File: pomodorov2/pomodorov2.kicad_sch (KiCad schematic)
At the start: 13 parts, among them J1 USB_B_Micro, J2 TC2050-IDC, J3 SOICbite, J4 Stemma, U1 MDBT50Q-1MV2, Y1 32.768kHz

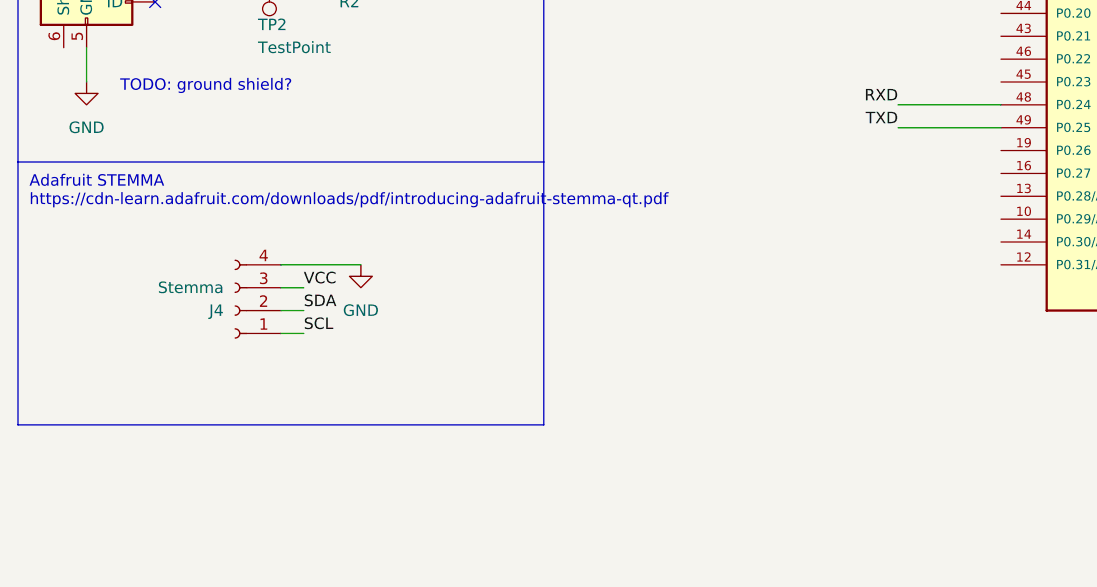
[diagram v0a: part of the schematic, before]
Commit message: Populate parts on board, remove stemma conn 🪓
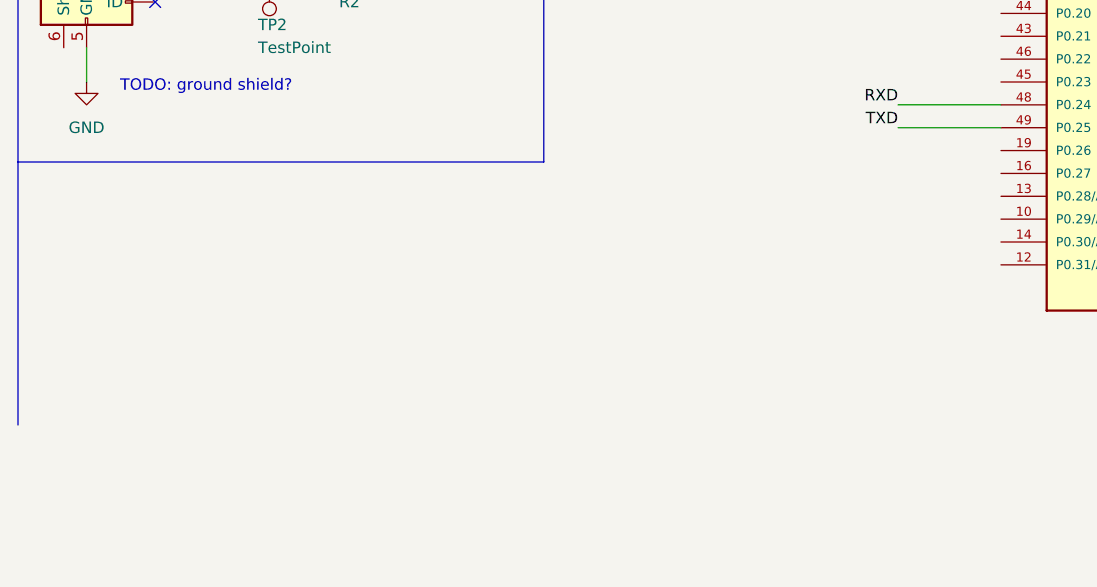
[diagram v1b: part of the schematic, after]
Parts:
- removed J4: Stemma, Connector_JST:JST_PH_S4B-PH-K_1x04_P2.00mm_Horizontal, symbol Connector:Conn_01x04_Female
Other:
- note removed: "Adafruit STEMMA https://cdn-learn.adafruit.com/downloads/pdf/introducing-adafruit-stemma-qt.pdf"
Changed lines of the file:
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@@
-    (stroke (width 0) (type default) (color 0 0 0 0))
-  )
-  (wire (pts (xy 40.64 133.35) (xy 43.18 133.35))
     (stroke (width 0) (type default) (color 0 0 0 0))
   )
@@
     (stroke (width 0) (type default) (color 0 0 0 0))
   )
-  (polyline (pts (xy 69.85 148.59) (xy 69.85 119.38))
-    (stroke (width 0) (type default) (color 0 0 0 0))
-  )
   (wire (pts (xy 109.22 97.79) (xy 120.65 97.79))
     (stroke (width 0) (type default) (color 0 0 0 0))
@@
     (stroke (width 0) (type default) (color 0 0 0 0))
   )
-  (polyline (pts (xy 11.43 148.59) (xy 69.85 148.59))
-    (stroke (width 0) (type default) (color 0 0 0 0))
-  )
   (wire (pts (xy 97.79 46.99) (xy 93.98 46.99))
     (stroke (width 0) (type default) (color 0 0 0 0))
   )
-  (wire (pts (xy 40.64 138.43) (xy 43.18 138.43))
-    (stroke (width 0) (type default) (color 0 0 0 0))
-  )
   (wire (pts (xy 26.67 24.13) (xy 33.02 24.13))
     (stroke (width 0) (type default) (color 0 0 0 0))
@@
     (stroke (width 0) (type default) (color 0 0 0 0))
   )
-  (wire (pts (xy 40.64 135.89) (xy 43.18 135.89))
-    (stroke (width 0) (type default) (color 0 0 0 0))
-  )
   (wire (pts (xy 26.67 67.31) (xy 26.67 72.39))
     (stroke (width 0) (type default) (color 0 0 0 0))
@@
     (stroke (width 0) (type default) (color 0 0 0 0))
   )
-  (wire (pts (xy 40.64 130.81) (xy 49.53 130.81))
-    (stroke (width 0) (type default) (color 0 0 0 0))
-  )
   (text "Maybe ground\n(or N/C)" (at 12.7 73.66 0)
     (effects (font (size 1.27 1.27)) (justify left bottom))
@@
   )
   (text "April 10, 2022" (at 207.01 194.31 0)
-    (effects (font (size 1.27 1.27)) (justify left bottom))
-  )
-  (text "Adafruit STEMMA\nhttps://cdn-learn.adafruit.com/downloads/pdf/introducing-adafruit-stemma-qt.pdf"
-    (at 12.7 124.46 0)
     (effects (font (size 1.27 1.27)) (justify left bottom))
   )
@@
     (effects (font (size 1.27 1.27)) (justify left bottom))
   )
-  (label "SDA" (at 43.18 135.89 0)
-    (effects (font (size 1.27 1.27)) (justify left bottom))
-  )
   (label "MISO" (at 109.22 90.17 180)
     (effects (font (size 1.27 1.27)) (justify right bottom))
-  )
-  (label "SCL" (at 43.18 138.43 0)
-    (effects (font (size 1.27 1.27)) (justify left bottom))
-  )
-  (label "VCC" (at 43.18 133.35 0)
-    (effects (font (size 1.27 1.27)) (justify left bottom))
   )
   (label "RXD" (at 109.22 113.03 180)
@@
     )
     (pin "1")
-  )
-  (symbol (lib_id "Connector:Conn_01x04_Female") (at 35.56 135.89 180) (unit 1)
-    (in_bom yes) (on_board yes) (fields_autoplaced)
-    (property "Reference" "J4" (id 0) (at 34.29 135.8901 0)
-      (effects (font (size 1.27 1.27)) (justify left))
-    )
-    (property "Value" "Stemma" (id 1) (at 34.29 133.3501 0)
-      (effects (font (size 1.27 1.27)) (justify left))
-    )
-    (property "Footprint" "Connector_JST:JST_PH_S4B-PH-K_1x04_P2.00mm_Horizontal" (id 2) (at 35.56 135.89 0)
-      (effects (font (size 1.27 1.27)) hide)
-    )
-    (property "Datasheet" "~" (id 3) (at 35.56 135.89 0)
-      (effects (font (size 1.27 1.27)) hide)
-    )
-    (pin "1")
-    (pin "2")
-    (pin "3")
-    (pin "4")
   )
   (symbol (lib_id "Device:L") (at 182.88 46.99 90) (unit 1)
@@
     (pin "1")
   )
-  (symbol (lib_id "power:GND") (at 49.53 130.81 0) (unit 1)
-    (in_bom yes) (on_board yes) (fields_autoplaced)
-    (property "Reference" "#PWR0110" (id 0) (at 49.53 137.16 0)
-      (effects (font (size 1.27 1.27)) hide)
-    )
-    (property "Value" "GND" (id 1) (at 49.53 135.89 0))
-    (property "Footprint" "" (id 2) (at 49.53 130.81 0)
-      (effects (font (size 1.27 1.27)) hide)
-    )
-    (property "Datasheet" "" (id 3) (at 49.53 130.81 0)
-      (effects (font (size 1.27 1.27)) hide)
-    )
-    (pin "1")
-  )
   (symbol (lib_id "Device:C") (at 101.6 46.99 90) (unit 1)
     (in_bom yes) (on_board yes)
@@
       (reference "#PWR0109") (unit 1) (value "VCC") (footprint "")
     )
-    (path "/b743f14b-92cb-4fa5-800d-537d59776f96"
-      (reference "#PWR0110") (unit 1) (value "GND") (footprint "")
-    )
     (path "/befd62b1-619b-4572-9ca1-684dbc340252"
       (reference "C1") (unit 1) (value "22pF") (footprint "Capacitor_SMD:C_0805_2012Metric_Pad1.18x1.45mm_HandSolder")
@@
       (reference "J3") (unit 1) (value "SOICbite") (footprint "SOICbite:SOIC_clipProgSmall")
     )
-    (path "/06cdca5c-90eb-4dd4-b5aa-f29162564498"
-      (reference "J4") (unit 1) (value "Stemma") (footprint "Connector_JST:JST_PH_S4B-PH-K_1x04_P2.00mm_Horizontal")
-    )
     (path "/1076e783-93f7-46aa-bc23-aa8ec07a9cd9"
